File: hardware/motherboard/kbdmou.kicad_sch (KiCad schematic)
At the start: 17 parts, among them J13 DIN-5_180degree, J14 Mini-DIN-6, Q1 2N4403, Q2 FQP27P06, U21 ATmega8-16A

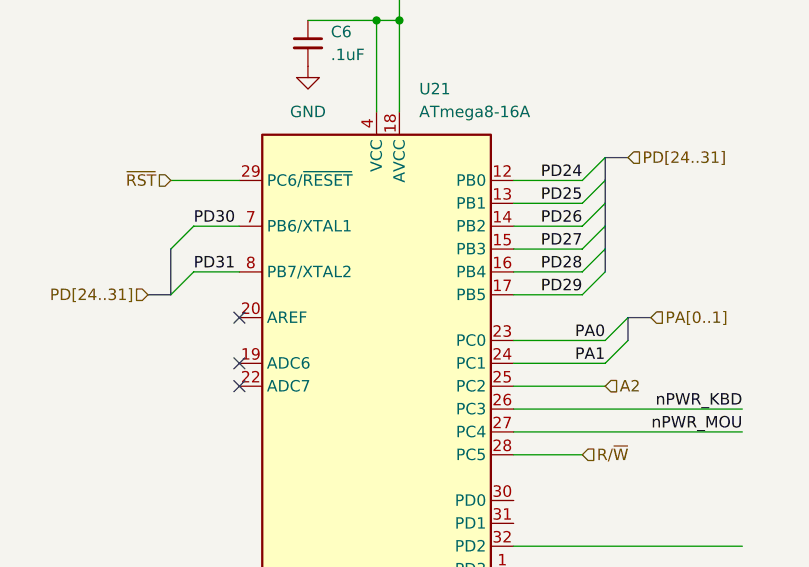
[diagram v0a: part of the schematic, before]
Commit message: restructure, create minimum board project
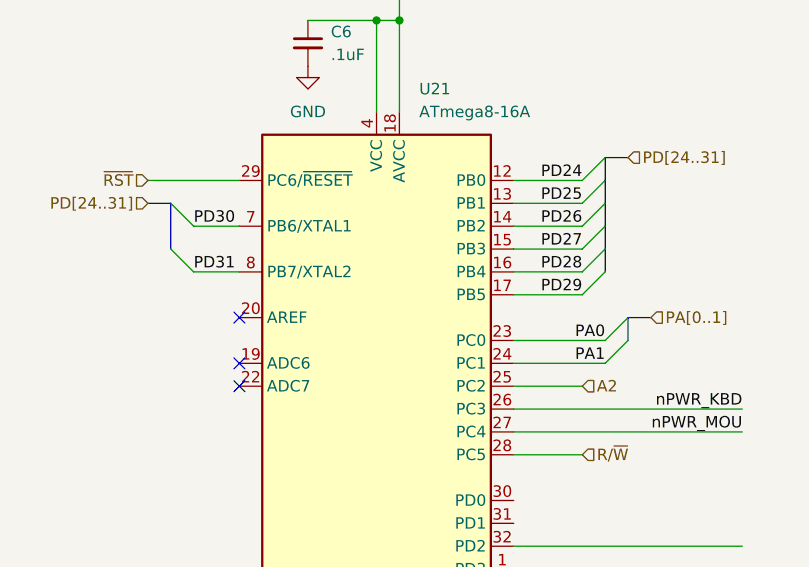
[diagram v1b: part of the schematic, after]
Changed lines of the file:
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@@
     (stroke (width 0) (type default))
   )
-  (bus_entry (at 58.42 119.38) (size 2.54 -2.54)
-    (stroke (width 0) (type default))
-  )
-  (bus_entry (at 58.42 114.3) (size 2.54 -2.54)
+  (bus_entry (at 58.42 109.22) (size 2.54 2.54)
+    (stroke (width 0) (type default))
+  )
+  (bus_entry (at 58.42 114.3) (size 2.54 2.54)
     (stroke (width 0) (type default))
   )
@@
     (stroke (width 0) (type default))
   )
-  (wire (pts (xy 96.52 129.54) (xy 106.68 129.54))
+  (wire (pts (xy 96.52 129.54) (xy 104.14 129.54))
     (stroke (width 0) (type default))
   )
@@
     (stroke (width 0) (type default))
   )
-  (bus (pts (xy 55.88 119.38) (xy 58.42 119.38))
+  (bus (pts (xy 55.88 109.22) (xy 58.42 109.22))
     (stroke (width 0) (type default))
   )
@@
     (stroke (width 0) (type default))
   )
-  (wire (pts (xy 58.42 106.68) (xy 66.04 106.68))
+  (wire (pts (xy 55.88 106.68) (xy 66.04 106.68))
     (stroke (width 0) (type default))
   )
@@
     (stroke (width 0) (type default))
   )
-  (bus (pts (xy 58.42 114.3) (xy 58.42 119.38))
+  (bus (pts (xy 58.42 114.3) (xy 58.42 109.22))
     (stroke (width 0) (type default))
   )
@@
     (effects (font (size 1.27 1.27)) (justify left))
   )
-  (hierarchical_label "A2" (shape input) (at 106.68 129.54 0) (fields_autoplaced)
+  (hierarchical_label "A2" (shape input) (at 104.14 129.54 0) (fields_autoplaced)
     (effects (font (size 1.27 1.27)) (justify left))
   )
@@
     (effects (font (size 1.27 1.27)) (justify left))
   )
-  (hierarchical_label "~{RST}" (shape input) (at 58.42 106.68 180) (fields_autoplaced)
+  (hierarchical_label "~{RST}" (shape input) (at 55.88 106.68 180) (fields_autoplaced)
     (effects (font (size 1.27 1.27)) (justify right))
   )
@@
     (effects (font (size 1.27 1.27)) (justify left))
   )
-  (hierarchical_label "PD[24..31]" (shape input) (at 55.88 119.38 180) (fields_autoplaced)
+  (hierarchical_label "PD[24..31]" (shape input) (at 55.88 109.22 180) (fields_autoplaced)
     (effects (font (size 1.27 1.27)) (justify right))
   )

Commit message: work on testboard, move 3d models
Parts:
- renumbered C2 to C1, C1 to C2, F2 to F1, F1 to F2, J14 to J6, J13 to J7
